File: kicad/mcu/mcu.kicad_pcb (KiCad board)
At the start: 2 copper layers, 49 x 42 mm, 23 parts, among them J1 Conn_01x05, J2 Conn_01x04, Q1 BC817, U1 AMS1117-3.3, U2 STM32F030F4Px

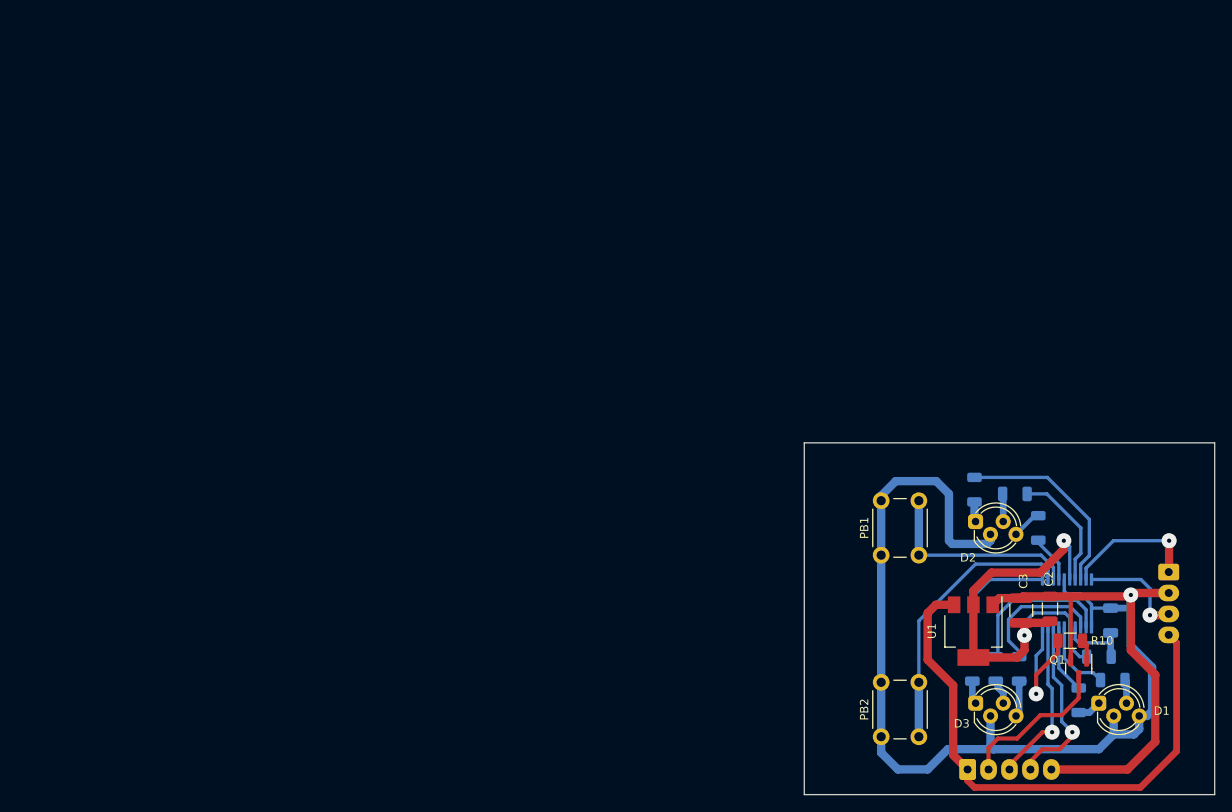
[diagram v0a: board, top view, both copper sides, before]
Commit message: Поробуем на плате разместить eeprom
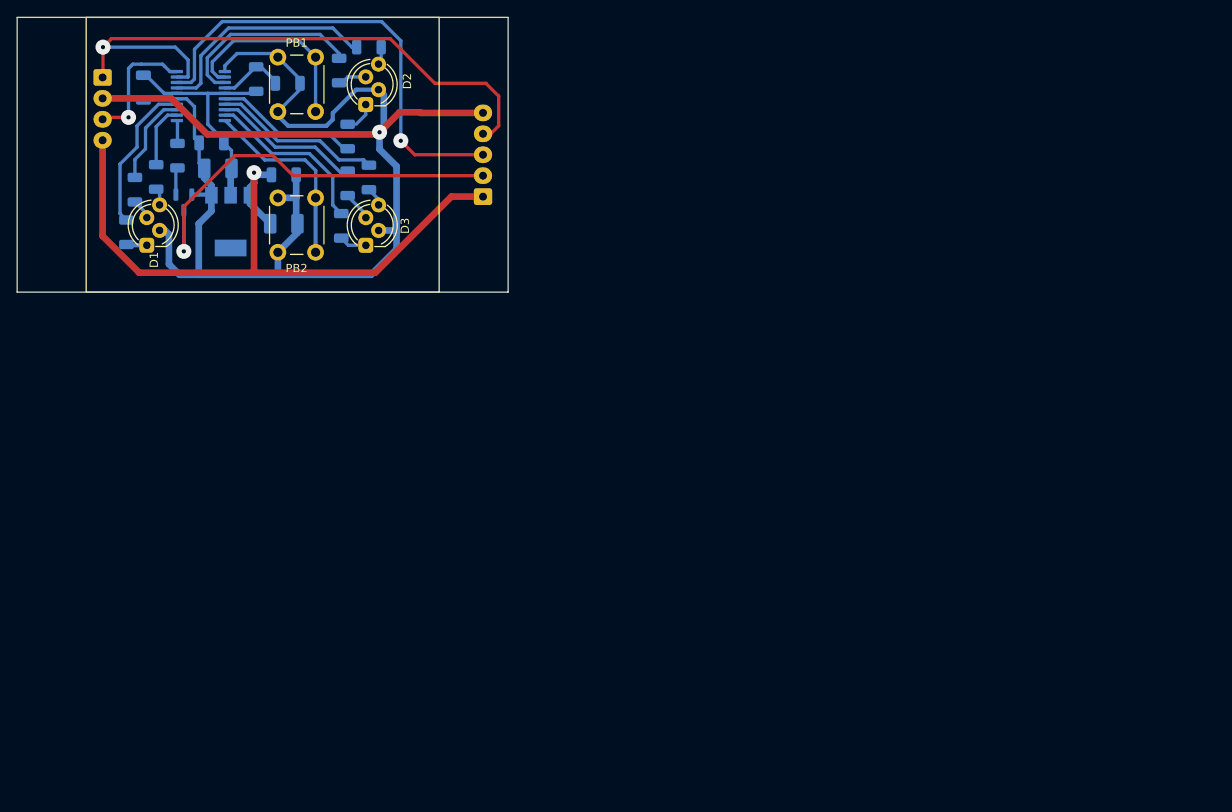
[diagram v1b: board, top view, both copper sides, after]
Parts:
- added C4: 0.1, Capacitor_SMD:C_1206_3216Metric, B.Cu at (31.8, 18.8)
- added C5: 0.1, Capacitor_SMD:C_1206_3216Metric, B.Cu at (15.1, 8.38)
- added C6: 100.0x6.3V, Capacitor_Tantalum_SMD:CP_EIA-3528-21_Kemet-B_Pad1.50x2.35mm_HandSolder, B.Cu at (31.8, 24.6)
- added R11: 64, Resistor_SMD:R_1206_3216Metric, B.Cu at (16.6, 19.1)
- C2: value C -> 0.1; moved to B.Cu
- C3: value C_Polarized -> 100.0x6.3V; footprint Capacitor_SMD:C_1210_3225Metric -> Capacitor_Tantalum_SMD:CP_EIA-3528-21_Kemet-B_Pad1.50x2.35mm_HandSolder; moved to B.Cu
- Q1: moved to B.Cu
- R10: value 224 -> 1k; moved to B.Cu
- U1: value AMS1117-3.3 -> LM1117-3.3; footprint Package_TO_SOT_SMD:SOT-223-3_TabPin2 -> Package_TO_SOT_SMD:SOT-223; moved to B.Cu
- moved J2 140.3 mm to (10.2, 7.17)
- moved R2 130.6 mm to (14.1, 20.6), turned to -90 degrees
- moved R3 126.7 mm to (13.0, 25.7)
- moved D1 126.1 mm to (15.5, 27.2), turned to 90 degrees
- moved R1 122.0 mm to (28.5, 7.37), turned to 90 degrees
- moved R10 121.3 mm to (19.1, 16.5), turned to -90 degrees
- moved Q1 120.5 mm to (19.9, 22.1)
- moved U2 119.9 mm to (21.9, 9.40), turned to 180 degrees
- moved C1 117.3 mm to (32.3, 7.87), turned to 180 degrees
- moved C2 114.5 mm to (23.2, 15.0), turned to 180 degrees
- moved C3 109.5 mm to (24.0, 18.0), turned to 180 degrees
- moved U1 101.3 mm to (25.5, 24.4)
- moved R4 98.4 mm to (42.0, 3.56), turned to 0 degrees
- moved R7 97.3 mm to (42.0, 19.1)
- moved R8 96.7 mm to (39.5, 19.8)
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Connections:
- D1 pad 4: GNDD -> Net-(D1-Pad4)
- J1 pad 4: /SENS2 -> /SWDIO
- PB1 pad 2: /PB2 -> /PB1
- PB2 pad 2: /PB1 -> /PB2
- R2 pad 1: /RELE_LED1 -> /RELE_LED2
- R3 pad 1: /RELE_LED2 -> /RELE_LED1
- R4 pad 1: /LED2_1 -> /LED2_3
- R6 pad 1: /LED2_3 -> /LED2_1
- R7 pad 1: /LED3_2 -> /LED3_3
- R8 pad 1: /LED3_3 -> /LED3_2
- U2 pad 10: /RELE -> /PB2
- U2 pad 11: /LED3_1 -> /RELE
- U2 pad 12: /PB1 -> /RELE_LED3
- U2 pad 13: /PB2 -> /RELE_LED2
- U2 pad 14: /LED2_1 -> /RELE_LED1
- U2 pad 17: /LED2_2 -> /LED2_3
- U2 pad 18: /LED2_3 -> /SENS1
- U2 pad 2: /LED3_3 -> /PB1
- U2 pad 3: /LED3_2 -> /LED2_2
- U2 pad 6: /RELE_LED1 -> /LED2_1
- U2 pad 7: /RELE_LED2 -> /LED3_3
- U2 pad 8: /SENS2 -> /LED3_2
- U2 pad 9: /SENS1 -> /LED3_1
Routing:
- net /SWDIO: track 16.4 -> 74.0 mm
- net /SENS1: track 19.9 -> 55.2 mm
- net /RELE_OUT: track 18.4 -> 49.5 mm, vias 0 -> 1
- net +3.3V: track 53.8 -> 27.8 mm, vias 2 -> 0
- net /SENS2: track 21.2 -> 0.00 mm, vias 1 -> 0
- net VDD: track 66.9 -> 84.0 mm, vias 0 -> 1
- net /RELE: track 15.7 -> 2.75 mm, vias 1 -> 0
- net /LED2_1: track 5.71 -> 16.8 mm
- net /PB1: track 33.4 -> 23.6 mm
- net /RELE_LED1: track 9.08 -> 18.2 mm
- net /LED2_2: track 14.5 -> 22.9 mm
- net /RELE_LED3: track 0.00 -> 7.58 mm
- net /LED3_1: track 16.4 -> 20.7 mm
- net /LED2_3: track 23.4 -> 27.3 mm
- net /RELE_LED2: track 8.21 -> 11.1 mm
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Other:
- board size 49 x 42 mm -> 58.6 x 32.8 mm

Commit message: пока без eeprom
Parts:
- added PB3: Reset, кнопки:PB_SMD_3x6x2.5, F.Cu at (240.5, 25.6)
- C1: value C -> 0.1
- R1: value R -> 10k
- R11, R4, R7: value 64 -> 62
- R2, R5, R8: value 104 -> 100
- R3, R6, R9: value 224 -> 220
- U1: footprint Package_TO_SOT_SMD:SOT-223 -> Package_TO_SOT_SMD:SOT-223-3_TabPin2
- U2: value STM32F030F4Px -> STM32F030F4P6
- moved J2 218.9 mm to (228.4, 25.4)
- moved R6 218.7 mm to (257.4, 32.4)
- moved R1 218.4 mm to (246.1, 26.2)
- moved C1 218.2 mm to (249.8, 26.1)
- moved C5 218.0 mm to (232.5, 24.9)
- moved D1 217.8 mm to (232.6, 45.4)
- moved R8 217.8 mm to (256.5, 38.0)
- moved U2 217.8 mm to (239.0, 27.6)
- moved C2 217.8 mm to (240.3, 33.2)
- moved C3 217.8 mm to (241.0, 36.2)
- moved C4 217.8 mm to (248.9, 37.0)
- moved C6 217.8 mm to (248.9, 42.8)
- moved D2 217.8 mm to (258.7, 28.6)
- moved D3 217.8 mm to (258.7, 45.4)
- moved PB1 217.8 mm to (248.2, 29.4)
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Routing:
- net GNDD: track 181.8 -> 192.1 mm
- net +3.3V: track 27.8 -> 36.3 mm
- net /RELE_OUT: track 49.5 -> 41.2 mm
- net Net-(C1-Pad2): track 8.04 -> 15.4 mm, vias 0 -> 1
- net VDD: track 84.0 -> 77.7 mm
- net /SWDIO: track 74.0 -> 68.1 mm
- net /SENS1: track 55.2 -> 50.9 mm
- net /SWGCLK: track 15.4 -> 18.1 mm
- net /LED2_3: track 27.3 -> 28.9 mm
- net /LED2_1: track 16.8 -> 18.0 mm
- net /PB1: track 23.6 -> 24.5 mm
- net /RELE_LED1: track 18.2 -> 18.8 mm
- net (no net): vias 0 -> 4
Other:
- board size 58.6 x 32.8 mm -> 42.1 x 32.8 mm
